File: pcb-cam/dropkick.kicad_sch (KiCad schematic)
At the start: 50 parts, among them J1 Conn_01x10, SW1 450405020524, SW2 KMR211NG_LFS, U1 SPX3819-3.3, U2 MCP73831T-2ACI/OT, U3 CAM-M8C-0, U4 ATSAMD21G18A-AUT, U5 DPS310XTSA1, U6 MPU-6050, X1 USB micro-B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

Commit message: Add mfr info
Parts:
- U6: footprint QFN24_4MM_SMSC -> lib_fp:MPU6XXX_QFN24_4MM_SMSC
- X1: footprint 4UCONN_20329_V2 -> lib_fp:4UCONN_20329_V2
- X2: Manufacturer Part (none) -> S2B-PH-SM4-TB
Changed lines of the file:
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@@
+      (effects (font (size 1.27 1.27)) hide)
+    )
+    (property "Manufacturer Part" "S2B-PH-SM4-TB" (id 4) (at 78.74 46.99 0)
       (effects (font (size 1.27 1.27)) hide)
     )
@@
       (effects (font (size 1.27 1.0795)) (justify left bottom))
     )
-    (property "Footprint" "4UCONN_20329_V2" (id 2) (at 237.49 43.18 0)
+    (property "Footprint" "lib_fp:4UCONN_20329_V2" (id 2) (at 237.49 43.18 0)
       (effects (font (size 1.27 1.27)) hide)
     )
@@
       (effects (font (size 1.524 1.524)) hide)
     )
-    (property "Datasheet" "" (id 3) (at 349.25 91.44 0)
+    (property "Datasheet" "https://content.u-blox.com/sites/default/files/CAM-M8-FW3_DataSheet_%28UBX-15031574%29.pdf" (id 3) (at 349.25 91.44 0)
       (effects (font (size 1.524 1.524)))
     )
@@
       (effects (font (size 1.27 1.0795)) (justify left bottom))
     )
-    (property "Footprint" "QFN24_4MM_SMSC" (id 2) (at 234.95 224.79 0)
+    (property "Footprint" "lib_fp:MPU6XXX_QFN24_4MM_SMSC" (id 2) (at 234.95 224.79 0)
       (effects (font (size 1.27 1.27)) hide)
     )
@@
       (effects (font (size 1.524 1.524)) hide)
     )
-    (property "Datasheet" "" (id 3) (at 331.47 207.01 0)
-      (effects (font (size 1.524 1.524)))
+    (property "Datasheet" "https://www.infineon.com/dgdl/Infineon-DPS310-DS-v01_00-EN.pdf?fileId=5546d462576f34750157750826c42242" (id 3) (at 331.47 207.01 0)
+      (effects (font (size 1.524 1.524)) hide)
     )
     (property "Manufacturer Part" "DPS310XTSA1" (id 4) (at 331.47 207.01 0)
@@
     )
     (path "/b44eff6c-d37f-4e1f-9422-f8fd197ac6e5"
-      (reference "U6") (unit 1) (value "MPU-6050") (footprint "QFN24_4MM_SMSC")
+      (reference "U6") (unit 1) (value "MPU-6050") (footprint "lib_fp:MPU6XXX_QFN24_4MM_SMSC")
     )
     (path "/2c24724c-3e0f-486d-8577-a92c36e9b2e3"
-      (reference "X1") (unit 1) (value "USB micro-B") (footprint "4UCONN_20329_V2")
+      (reference "X1") (unit 1) (value "USB micro-B") (footprint "lib_fp:4UCONN_20329_V2")
     )
     (path "/27a17605-e78a-4939-884c-260b5756ef06"

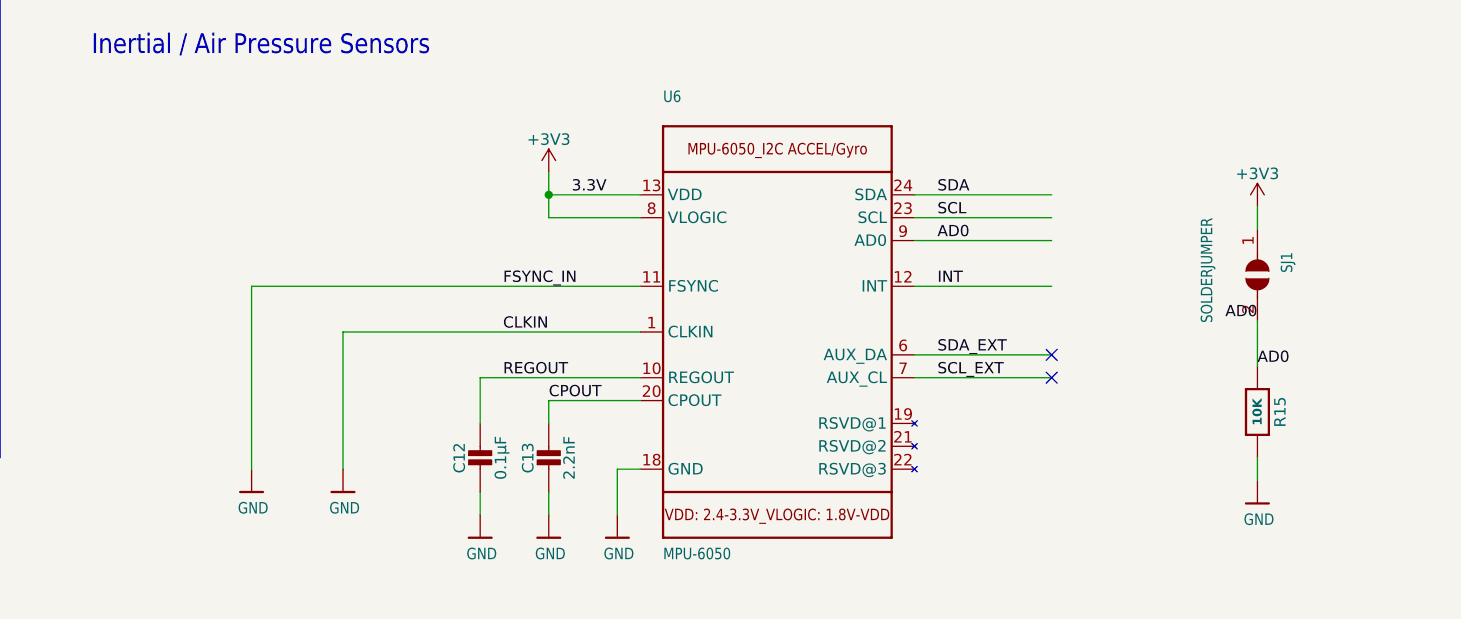
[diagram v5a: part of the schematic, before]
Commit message: Add VLOGIC bypass cap to 6050; update gerbers
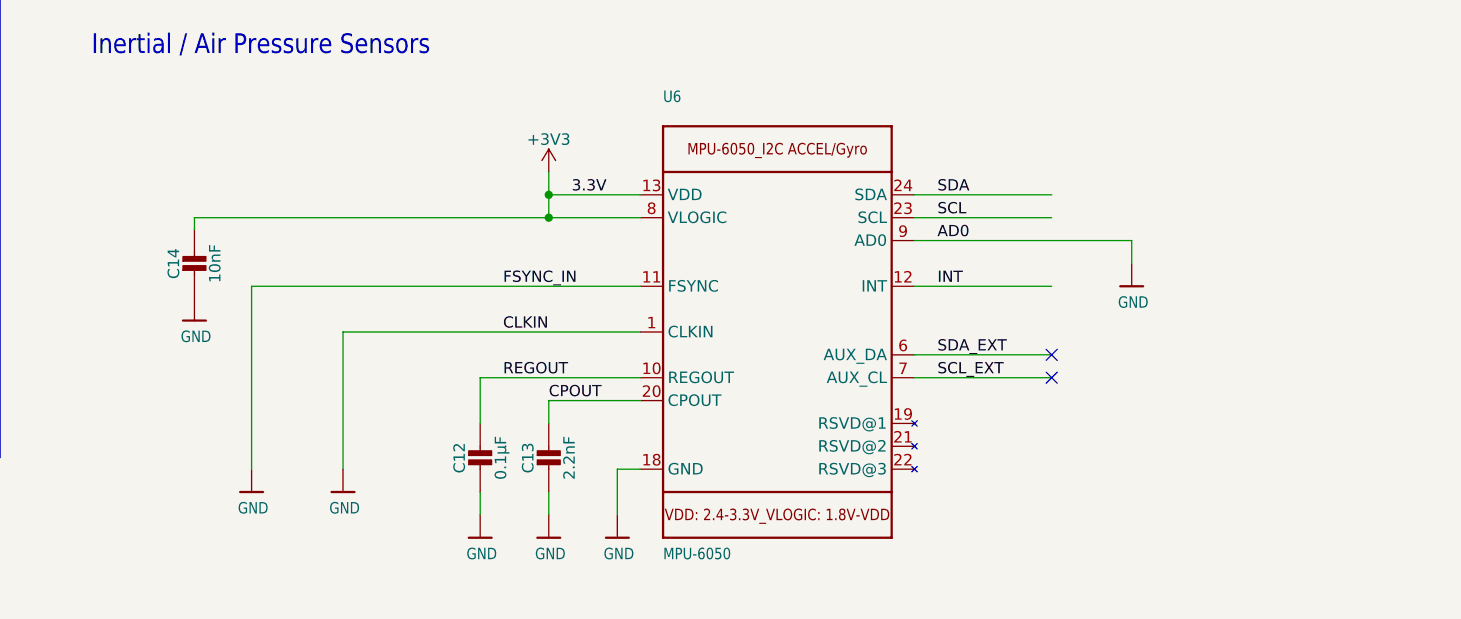
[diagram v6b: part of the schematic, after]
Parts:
- removed R15: 10K, Resistor_SMD:R_0603_1608Metric, symbol Adafruit MPU6050-eagle-import:RESISTOR_0603_NOOUT
- removed SJ1: SOLDERJUMPER, Resistor_SMD:R_0603_1608Metric, symbol Adafruit MPU6050-eagle-import:SOLDERJUMPER
- added C14: 10nF, Capacitor_SMD:C_0603_1608Metric, symbol Adafruit MPU6050-eagle-import:CAP_CERAMIC0603_NO
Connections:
- net AD0 is gone; now on net GND: U6.9 (AD0)
- net +3V3: now also C14.1
- net GND: now also C14.2
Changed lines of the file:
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@@
   (junction (at 318.77 209.55) (diameter 0) (color 0 0 0 0)
   )
+  (junction (at 209.55 212.09) (diameter 0) (color 0 0 0 0)
+  )
   (junction (at 283.21 83.82) (diameter 0) (color 0 0 0 0)
   )
@@
     (stroke (width 0) (type default) (color 0 0 0 0))
   )
+  (wire (pts (xy 209.55 212.09) (xy 170.18 212.09))
+    (stroke (width 0) (type default) (color 0 0 0 0))
+  )
   (wire (pts (xy 228.6 138.43) (xy 198.12 138.43))
     (stroke (width 0) (type default) (color 0 0 0 0))
@@
     (stroke (width 0) (type default) (color 0 0 0 0))
   )
-  (wire (pts (xy 288.29 238.76) (xy 288.29 241.3))
+  (wire (pts (xy 274.32 214.63) (xy 274.32 217.17))
     (stroke (width 0) (type default) (color 0 0 0 0))
   )
@@
     (stroke (width 0) (type default) (color 0 0 0 0))
   )
+  (wire (pts (xy 170.18 212.09) (xy 170.18 213.36))
+    (stroke (width 0) (type default) (color 0 0 0 0))
+  )
   (wire (pts (xy 132.08 106.68) (xy 114.3 106.68))
     (stroke (width 0) (type default) (color 0 0 0 0))
@@
     (stroke (width 0) (type default) (color 0 0 0 0))
   )
-  (wire (pts (xy 288.29 213.36) (xy 288.29 210.82))
-    (stroke (width 0) (type default) (color 0 0 0 0))
-  )
   (polyline (pts (xy 299.72 16.51) (xy 299.72 185.42))
     (stroke (width 0) (type default) (color 0 0 0 0))
@@
     (stroke (width 0) (type default) (color 0 0 0 0))
   )
-  (wire (pts (xy 288.29 223.52) (xy 288.29 228.6))
-    (stroke (width 0) (type default) (color 0 0 0 0))
-  )
   (wire (pts (xy 114.3 157.48) (xy 132.08 157.48))
     (stroke (width 0) (type default) (color 0 0 0 0))
@@
     (stroke (width 0) (type default) (color 0 0 0 0))
   )
-  (wire (pts (xy 250.19 214.63) (xy 265.43 214.63))
+  (wire (pts (xy 250.19 214.63) (xy 274.32 214.63))
     (stroke (width 0) (type default) (color 0 0 0 0))
   )
@@
     (effects (font (size 1.27 1.27)) (justify left bottom))
   )
-  (label "AD0" (at 288.29 228.6 0)
-    (effects (font (size 1.2446 1.2446)) (justify left bottom))
-  )
   (label "REGOUT" (at 204.47 229.87 0)
     (effects (font (size 1.2446 1.2446)) (justify left bottom))
@@
     (effects (font (size 1.2446 1.2446)) (justify left bottom))
   )
-  (label "AD0" (at 288.29 223.52 180)
-    (effects (font (size 1.2446 1.2446)) (justify right bottom))
-  )
   (label "SCL_EXT" (at 252.73 229.87 0)
     (effects (font (size 1.2446 1.2446)) (justify left bottom))
@@
     (pin "2")
   )
-  (symbol (lib_id "Adafruit MPU6050-eagle-import:RESISTOR_0603_NOOUT") (at 288.29 233.68 270) (unit 1)
+  (symbol (lib_id "Adafruit MPU6050-eagle-import:GND") (at 170.18 223.52 0) (unit 1)
     (in_bom yes) (on_board yes)
-    (property "Reference" "R15" (id 0) (at 290.83 233.68 0))
-    (property "Value" "10K" (id 1) (at 288.29 233.68 0)
-      (effects (font (size 1.016 1.016) bold))
-    )
-    (property "Footprint" "Resistor_SMD:R_0603_1608Metric" (id 2) (at 288.29 233.68 0)
+    (property "Reference" "#U$?" (id 0) (at 170.18 223.52 0)
       (effects (font (size 1.27 1.27)) hide)
     )
-    (property "Datasheet" "" (id 3) (at 288.29 233.68 0)
+    (property "Value" "GND" (id 1) (at 168.656 226.06 0)
+      (effects (font (size 1.27 1.0795)) (justify left bottom))
+    )
+    (property "Footprint" "" (id 2) (at 170.18 223.52 0)
       (effects (font (size 1.27 1.27)) hide)
     )
-    (property "Comments" "R11-R12 DNP" (id 4) (at 288.29 233.68 0)
+    (property "Datasheet" "" (id 3) (at 170.18 223.52 0)
       (effects (font (size 1.27 1.27)) hide)
     )
     (pin "1")
-    (pin "2")
   )
   (symbol (lib_id "Adafruit Feather M0 Adalogger-eagle-import:GND") (at 129.54 76.2 180) (unit 1)
@@
     (pin "1")
   )
-  (symbol (lib_id "Adafruit MPU6050-eagle-import:SOLDERJUMPER") (at 288.29 218.44 270) (unit 1)
-    (in_bom yes) (on_board yes)
-    (property "Reference" "SJ1" (id 0) (at 290.83 215.9 0)
-      (effects (font (size 1.27 1.0795)) (justify left bottom))
-    )
-    (property "Value" "SOLDERJUMPER" (id 1) (at 281.94 212.09 0)
-      (effects (font (size 1.27 1.0795)) (justify left bottom))
-    )
-    (property "Footprint" "Resistor_SMD:R_0603_1608Metric" (id 2) (at 288.29 218.44 0)
-      (effects (font (size 1.27 1.27)) hide)
-    )
-    (property "Datasheet" "" (id 3) (at 288.29 218.44 0)
-      (effects (font (size 1.27 1.27)) hide)
-    )
-    (pin "1")
-    (pin "2")
-  )
   (symbol (lib_id "Adafruit Ultimate GPS FeatherWing-eagle-import:GND") (at 349.25 162.56 0) (unit 1)
     (in_bom yes) (on_board yes)
@@
     (pin "MT2")
   )
-  (symbol (lib_id "Adafruit MPU6050-eagle-import:GND") (at 288.29 243.84 0) (unit 1)
+  (symbol (lib_id "Adafruit MPU6050-eagle-import:GND") (at 274.32 219.71 0) (unit 1)
     (in_bom yes) (on_board yes)
-    (property "Reference" "#U$028" (id 0) (at 288.29 243.84 0)
+    (property "Reference" "#U$028" (id 0) (at 274.32 219.71 0)
       (effects (font (size 1.27 1.27)) hide)
     )
-    (property "Value" "GND" (id 1) (at 286.766 246.38 0)
+    (property "Value" "GND" (id 1) (at 272.796 222.25 0)
       (effects (font (size 1.27 1.0795)) (justify left bottom))
     )
-    (property "Footprint" "" (id 2) (at 288.29 243.84 0)
+    (property "Footprint" "" (id 2) (at 274.32 219.71 0)
       (effects (font (size 1.27 1.27)) hide)
     )
-    (property "Datasheet" "" (id 3) (at 288.29 243.84 0)
+    (property "Datasheet" "" (id 3) (at 274.32 219.71 0)
       (effects (font (size 1.27 1.27)) hide)
     )
@@
     (pin "9")
   )
-  (symbol (lib_id "Adafruit Feather M0 Adalogger-eagle-import:GND") (at 22.86 59.69 0) (unit 1)
+  (symbol (lib_id "Adafruit MPU6050-eagle-import:CAP_CERAMIC0603_NO") (at 170.18 218.44 0) (unit 1)
     (in_bom yes) (on_board yes)
-    (property "Reference" "#U$06" (id 0) (at 22.86 59.69 0)
+    (property "Reference" "C14" (id 0) (at 167.89 217.19 90))
+    (property "Value" "10nF" (id 1) (at 172.48 217.19 90))
+    (property "Footprint" "Capacitor_SMD:C_0603_1608Metric" (id 2) (at 170.18 218.44 0)
       (effects (font (size 1.27 1.27)) hide)
     )
-    (property "Value" "GND" (id 1) (at 21.336 62.23 0)
-      (effects (font (size 1.778 1.5113)) (justify left bottom))
-    )
-    (property "Footprint" "" (id 2) (at 22.86 59.69 0)
+    (property "Datasheet" "" (id 3) (at 170.18 218.44 0)
       (effects (font (size 1.27 1.27)) hide)
     )
-    (property "Datasheet" "" (id 3) (at 22.86 59.69 0)
+    (property "Manufacturer Part" "C0603C222K1HACAUTO" (id 4) (at 170.18 218.44 0)
       (effects (font (size 1.27 1.27)) hide)
     )
     (pin "1")
+    (pin "2")
   )
-  (symbol (lib_id "power:+3V3") (at 288.29 210.82 0) (unit 1)
-    (in_bom yes) (on_board yes) (fields_autoplaced)
-    (property "Reference" "#PWR09" (id 0) (at 288.29 214.63 0)
+  (symbol (lib_id "Adafruit Feather M0 Adalogger-eagle-import:GND") (at 22.86 59.69 0) (unit 1)
+    (in_bom yes) (on_board yes)
+    (property "Reference" "#U$06" (id 0) (at 22.86 59.69 0)
       (effects (font (size 1.27 1.27)) hide)
     )
-    (property "Value" "+3V3" (id 1) (at 288.29 207.2155 0))
-    (property "Footprint" "" (id 2) (at 288.29 210.82 0)
+    (property "Value" "GND" (id 1) (at 21.336 62.23 0)
+      (effects (font (size 1.778 1.5113)) (justify left bottom))
+    )
+    (property "Footprint" "" (id 2) (at 22.86 59.69 0)
       (effects (font (size 1.27 1.27)) hide)
     )
-    (property "Datasheet" "" (id 3) (at 288.29 210.82 0)
+    (property "Datasheet" "" (id 3) (at 22.86 59.69 0)
       (effects (font (size 1.27 1.27)) hide)
     )
@@
       (reference "#PWR08") (unit 1) (value "+3V3") (footprint "")
     )
-    (path "/9037a4d5-1acc-4a4b-bc7b-892adc05cad5"
-      (reference "#PWR09") (unit 1) (value "+3V3") (footprint "")
-    )
     (path "/d07eaceb-e013-4d97-b698-a6570a1e4fbf"
       (reference "#PWR010") (unit 1) (value "GND") (footprint "")
@@
       (reference "#U$031") (unit 1) (value "GND") (footprint "")
     )
+    (path "/1992087b-382d-43cd-aa96-b6a978357a02"
+      (reference "#U$?") (unit 1) (value "GND") (footprint "")
+    )
     (path "/b9acbd06-bca7-4b43-96e5-af1fc70b26c4"
       (reference "B1") (unit 1) (value "CR1220") (footprint "CR1220-2")
@@
       (reference "C13") (unit 1) (value "2.2nF") (footprint "Capacitor_SMD:C_0603_1608Metric")
     )
+    (path "/89bb4a92-b1b5-42c6-a5c4-e6bfced6556a"
+      (reference "C14") (unit 1) (value "10nF") (footprint "Capacitor_SMD:C_0603_1608Metric")
+    )
     (path "/3c5c540c-f2b8-43e0-a682-33d4cb1f2236"
       (reference "CHG1") (unit 1) (value "ORANGE LED") (footprint "LED_SMD:LED_0603_1608Metric")
@@
       (reference "R14") (unit 1) (value "10K") (footprint "Resistor_SMD:R_0603_1608Metric")
     )
-    (path "/19fed19d-c653-4d29-9bef-1aecb59afc04"
-      (reference "R15") (unit 1) (value "10K") (footprint "Resistor_SMD:R_0603_1608Metric")
-    )
-    (path "/1d41875d-8419-4731-9a57-168ae69c4de4"
-      (reference "SJ1") (unit 1) (value "SOLDERJUMPER") (footprint "Resistor_SMD:R_0603_1608Metric")
-    )
     (path "/92bef28d-c11f-4149-ae27-34f9e91c5fec"

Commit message: Upgrade to KiCad 7
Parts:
- added C15: 0.1uF, Capacitor_SMD:C_0603_1608Metric, symbol Adafruit MPU6050-eagle-import:CAP_CERAMIC0603_NO
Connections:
- net +3V3: now also C15.1
- net GND: now also C15.2
- net D11 renamed INT
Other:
- note added: "D11"
- moved on the sheet: B1, C11, C12, C13, C14, C6, H1, H2, H3, J1, JP1, L1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
